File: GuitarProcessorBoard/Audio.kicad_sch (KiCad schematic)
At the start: 42 parts, among them U201 TLV320AIC3204, U202 TL074

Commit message: single-ended output working
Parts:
- R204: value 470k -> 51k
- R205: value 470k -> 100k
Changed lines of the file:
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@@
 	(label "InputNeg"
 		(at 62.738 82.042 0)
+		(fields_autoplaced yes)
 		(effects
 			(font
@@
 	(label "Wet"
 		(at 55.372 151.638 180)
+		(fields_autoplaced yes)
 		(effects
 			(font
@@
 	(label "Bias2"
 		(at 241.046 128.27 0)
+		(fields_autoplaced yes)
 		(effects
 			(font
@@
 	(label "Bias2"
 		(at 245.11 79.502 180)
+		(fields_autoplaced yes)
 		(effects
 			(font
@@
 	(label "InputPos"
 		(at 70.104 94.742 180)
+		(fields_autoplaced yes)
 		(effects
 			(font
@@
 	(label "DAC_OUT"
 		(at 141.732 64.008 0)
+		(fields_autoplaced yes)
 		(effects
 			(font
@@
 	(label "Wet"
 		(at 195.326 66.04 180)
+		(fields_autoplaced yes)
 		(effects
 			(font
@@
 	(label "Bias1"
 		(at 43.434 84.582 180)
+		(fields_autoplaced yes)
 		(effects
 			(font
@@
 	(label "Bias2"
 		(at 178.054 76.962 180)
+		(fields_autoplaced yes)
 		(effects
 			(font
@@
 	(label "Bias1"
 		(at 219.456 128.524 0)
+		(fields_autoplaced yes)
 		(effects
 			(font
@@
 	(label "DAC_OUT"
 		(at 55.372 144.78 180)
+		(fields_autoplaced yes)
 		(effects
 			(font
@@
 	(label "Bias1"
 		(at 43.942 116.84 180)
+		(fields_autoplaced yes)
 		(effects
 			(font
@@
 			)
 		)
-		(property "Value" "470k"
+		(property "Value" "51k"
 			(at 38.354 107.95 90)
 			(effects
@@
 		(fields_autoplaced yes)
 		(property "Reference" "R205"
-			(at 50.8 98.806 90)
-			(effects
-				(font
-					(size 1.27 1.27)
-				)
-			)
-		)
-		(property "Value" "470k"
-			(at 50.8 101.346 90)
-			(effects
-				(font
+			(at 50.8 99.06 90)
+			(effects
+				(font
+					(size 1.27 1.27)
+				)
+			)
+		)
+		(property "Value" "100k"
+			(at 50.8 101.6 90)
+			(effects
+				(font

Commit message: differential output stage
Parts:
- removed C217, C218: 100n, Capacitor_SMD:C_0805_2012Metric, symbol Device:C
- removed C219: 1u, Capacitor_SMD:C_0805_2012Metric, symbol Device:C
- removed R217: 1M, Resistor_SMD:R_0805_2012Metric, symbol Device:R_US
- removed R218, R219: 10k, Resistor_SMD:R_0805_2012Metric, symbol Device:R_US
- removed RV201: 100kB, Potentiometer_THT:Potentiometer_Alpha_RD901F-40-00D_Single_Vertical_CircularHoles, symbol Device:R_Potentiometer_US
- removed TP202: DAC, TestPoint:TestPoint_THTPad_D2.0mm_Drill1.0mm_VAL, symbol Connector:TestPoint
- added C208: 100n, Capacitor_SMD:C_0805_2012Metric, symbol Device:C
- C207: value 1u -> 4n7
- C214: value 1u -> 100n
- R213: value 47k -> 470k
- R214: value 47k -> 1k
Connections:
- net +3.3V: no longer C201.1, C202.1, C203.1, U201.26 (LDOIN), U201.30 (LDO_SEL), U201.6 (IOVDD)
- net Bias2: now also R213.1; no longer U202.3 (+), U202.5 (+)
- net FX_IN: no longer C207.1
- net FX_OUT: now also C215.2
- net GND: now also C207.2, R216.2
- net at R213.2: now also R211.2, R212.1, U202.6 (-)
- net at U201.23 (OUT_R): now also R214.1
- net at R214.2: now also C207.1, C208.1
- net at R215.1: now also C208.2
- net at R216.1: now also R215.2, U202.5 (+)
- net DAC_OUT: no longer names the net of R208.1, U201.22 (OUT_L)
- new net +3.3VA: C201.1, C202.1, C203.1, U201.26 (LDOIN), U201.30 (LDO_SEL), U201.6 (IOVDD)
- now unconnected: U202.2 (-)
- no-connect marks 11 -> 13
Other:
- note removed: "Wet/Dry"
- moved on the sheet: C212, C214, C215, R208, R211, R212, U202A, U202B

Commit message: schematic changes
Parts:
- removed TP203: WET, TestPoint:TestPoint_THTPad_D2.0mm_Drill1.0mm_VAL, symbol Connector:TestPoint
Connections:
- net +3.3V is gone; now on net +3.3VA: R201.1, R202.1
- net Bias2: now also R216.2, U202.1, U202.2 (-); no longer R209.2, R210.1
- net GND: no longer R216.2
- net at U202.3 (+): now also R209.2, R210.1
- no-connect marks 13 -> 10
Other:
- moved on the sheet: R202, R203, R209, R210, R216, U202A

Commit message: differential output sim
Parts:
- removed R213: 470k, Resistor_SMD:R_0805_2012Metric, symbol Device:R_US
- R211: value 470k -> 100k
- R212, R215: value 470k -> 51k
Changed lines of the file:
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@@
 	)
 	(junction
-		(at 179.324 46.99)
-		(diameter 0)
-		(color 0 0 0 0)
-	)
-	(junction
 		(at 257.048 125.73)
 		(diameter 0)
@@
 	(wire
 		(pts
-			(xy 165.1 46.99) (xy 169.672 46.99)
-		)
-		(stroke
-			(width 0)
-			(type default)
-		)
-	)
-	(wire
-		(pts
 			(xy 195.58 136.144) (xy 195.58 137.16)
 		)
@@
 	(wire
 		(pts
-			(xy 177.292 46.99) (xy 179.324 46.99)
-		)
-		(stroke
-			(width 0)
-			(type default)
-		)
-	)
-	(wire
-		(pts
 			(xy 58.674 71.882) (xy 58.674 82.042)
 		)
@@
 	(label "InputNeg"
 		(at 62.738 82.042 0)
-		(fields_autoplaced yes)
 		(effects
 			(font
@@
 	(label "Bias2"
 		(at 259.08 125.73 0)
-		(fields_autoplaced yes)
 		(effects
 			(font
@@
 	(label "InputPos"
 		(at 70.104 94.742 180)
-		(fields_autoplaced yes)
 		(effects
 			(font
@@
 	(label "Bias2"
 		(at 179.324 77.978 270)
-		(fields_autoplaced yes)
 		(effects
 			(font
@@
 	(label "Wet"
 		(at 196.85 46.99 180)
-		(fields_autoplaced yes)
 		(effects
 			(font
@@
 	(label "Bias1"
 		(at 43.434 84.582 180)
-		(fields_autoplaced yes)
-		(effects
-			(font
-				(size 1.27 1.27)
-			)
-			(justify right bottom)
-		)
-	)
-	(label "Bias2"
-		(at 165.1 46.99 180)
-		(fields_autoplaced yes)
 		(effects
 			(font
@@
 	(label "Bias1"
 		(at 210.312 128.524 0)
-		(fields_autoplaced yes)
 		(effects
 			(font
@@
 	(label "Bias1"
 		(at 43.942 116.84 180)
-		(fields_autoplaced yes)
 		(effects
 			(font
@@
 		(fields_autoplaced yes)
 		(property "Reference" "R215"
-			(at 173.99 60.706 90)
+			(at 173.99 60.96 90)
 			(effects
 				(font
@@
 			)
 		)
-		(property "Value" "470k"
-			(at 173.99 63.246 90)
+		(property "Value" "51k"
+			(at 173.99 63.5 90)
 			(effects
 				(font
@@
 			)
 		)
-		(property "Value" "470k"
+		(property "Value" "100k"
 			(at 173.736 53.34 90)
 			(effects
@@
 			)
 		)
-		(property "Value" "470k"
+		(property "Value" "51k"
 			(at 186.944 43.18 90)
 			(effects
@@
 					(unit 1)
 				)
-			)
-		)
-	)
-	(symbol
-		(lib_id "Device:R_US")
-		(at 173.482 46.99 90)
-		(unit 1)
-		(exclude_from_sim no)
-		(in_bom yes)
-		(on_board yes)
-		(dnp no)
-		(fields_autoplaced yes)
-		(property "Reference" "R213"
-			(at 173.482 40.64 90)
-			(effects
-				(font
-					(size 1.27 1.27)
-				)
-			)
-		)
-		(property "Value" "470k"
-			(at 173.482 43.18 90)
-			(effects
-				(font
-					(size 1.27 1.27)
-				)
-			)
-		)
-		(property "Footprint" "Resistor_SMD:R_0805_2012Metric"
-			(at 173.736 45.974 90)
-			(effects
-				(font
-					(size 1.27 1.27)
-				)
-				(hide yes)
-			)
-		)
-		(property "Datasheet" "~"
-			(at 173.482 46.99 0)
-			(effects
-				(font
-					(size 1.27 1.27)
-				)
-				(hide yes)
-			)
-		)
-		(property "Description" "Resistor, US symbol"
-			(at 173.482 46.99 0)
-			(effects
-				(font
-					(size 1.27 1.27)
-				)
-				(hide yes)
-			)
-		)
-		(pin "1"
-		)
-		(pin "2"
-		)
-		(instances
-			(project "GuitarProcessorBoard"
-				(path "/524c695b-c632-4089-9e9a-ef0f89cad1b2/ef3a9a4a-abe1-4d77-855c-3594c7f88930"
-					(reference "R213")
-					(unit 1)
-				)

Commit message: routing start
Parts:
- C215: value 1u -> 100n
- R215: value 51k -> 100k
- R216: value 470k -> 51k
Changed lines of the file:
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@@
 			)
 		)
-		(property "Value" "51k"
+		(property "Value" "100k"
 			(at 173.99 63.5 90)
 			(effects
@@
 			)
 		)
-		(property "Value" "1u"
+		(property "Value" "100n"
 			(at 202.692 54.61 90)
 			(effects
@@
 		(fields_autoplaced yes)
 		(property "Reference" "R216"
-			(at 181.864 71.8819 0)
+			(at 181.61 71.8819 0)
 			(effects
 				(font
@@
 			)
 		)
-		(property "Value" "470k"
-			(at 181.864 74.4219 0)
-			(effects
-				(font
+		(property "Value" "51k"
+			(at 181.61 74.4219 0)
+			(effects
+				(font

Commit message: DRC passing
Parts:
- C209: value 1u -> 100n
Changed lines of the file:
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@@
 		(fields_autoplaced yes)
 		(property "Reference" "C209"
-			(at 28.448 104.648 90)
+			(at 28.448 104.14 90)
 			(effects
 				(font
@@
 			)
 		)
-		(property "Value" "1u"
-			(at 28.448 107.188 90)
+		(property "Value" "100n"
+			(at 28.448 106.68 90)
 			(effects
 				(font

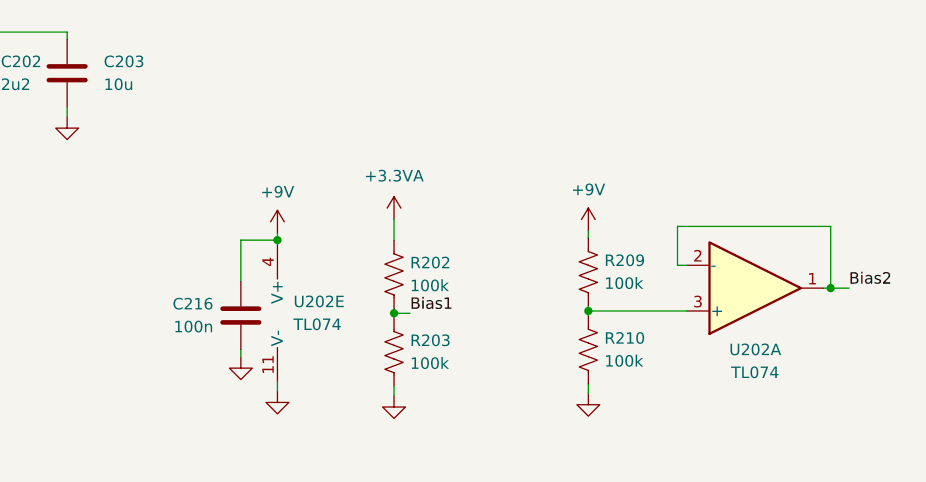
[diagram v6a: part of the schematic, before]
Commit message: split PSU schematic, DRC passing
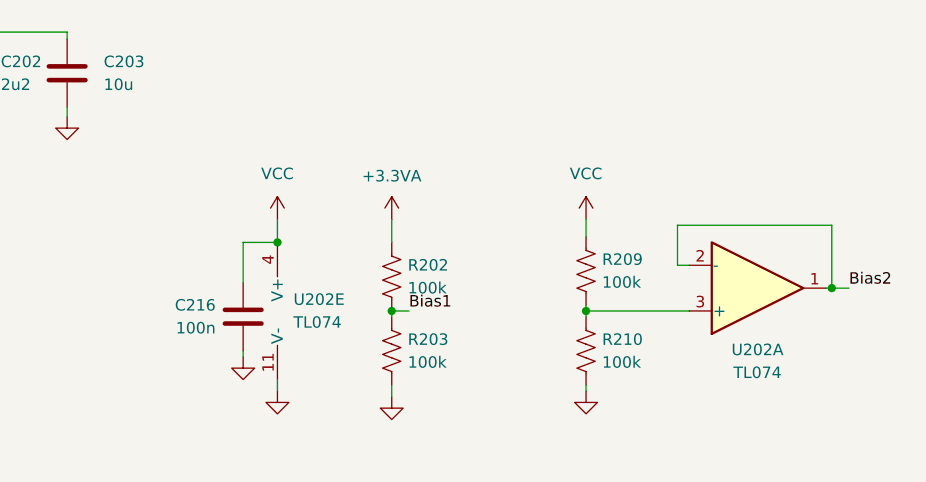
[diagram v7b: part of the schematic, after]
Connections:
- net +9V renamed VCC
